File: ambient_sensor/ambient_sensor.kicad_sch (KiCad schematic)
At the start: 13 parts, among them J1 Conn_01x02_Pin, U4 ATmega328-P, U6 LD1117S33TR_SOT223, Y1 Crystal

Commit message: sensors connected
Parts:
- removed R1: 4.7k, symbol Device:R
- removed R2: 4.7k, Resistor_SMD:R_1206_3216Metric, symbol Device:R
- added BT1: Battery, Battery:BatteryHolder_Keystone_2479_3xAAA, symbol Device:Battery
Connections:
- net +4V: no longer U3.2 (3Vo)
- net GND: now also BT1.2 (-)
- net SDA: now reaches U2. (VIN), U4.27 (PC4)
- net SDA: now also U1.2 (SDA), U3.6 (SDI)
- net SCL: now reaches U1.3 (SCL), U2. (VIN), U4.28 (PC5)
- net SCL: now also U3.4 (SCK); no longer U3.5 (SDO)
- net at U6.3 (VI): now also BT1.1 (+)
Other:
- moved on the sheet: U1, U2, U3

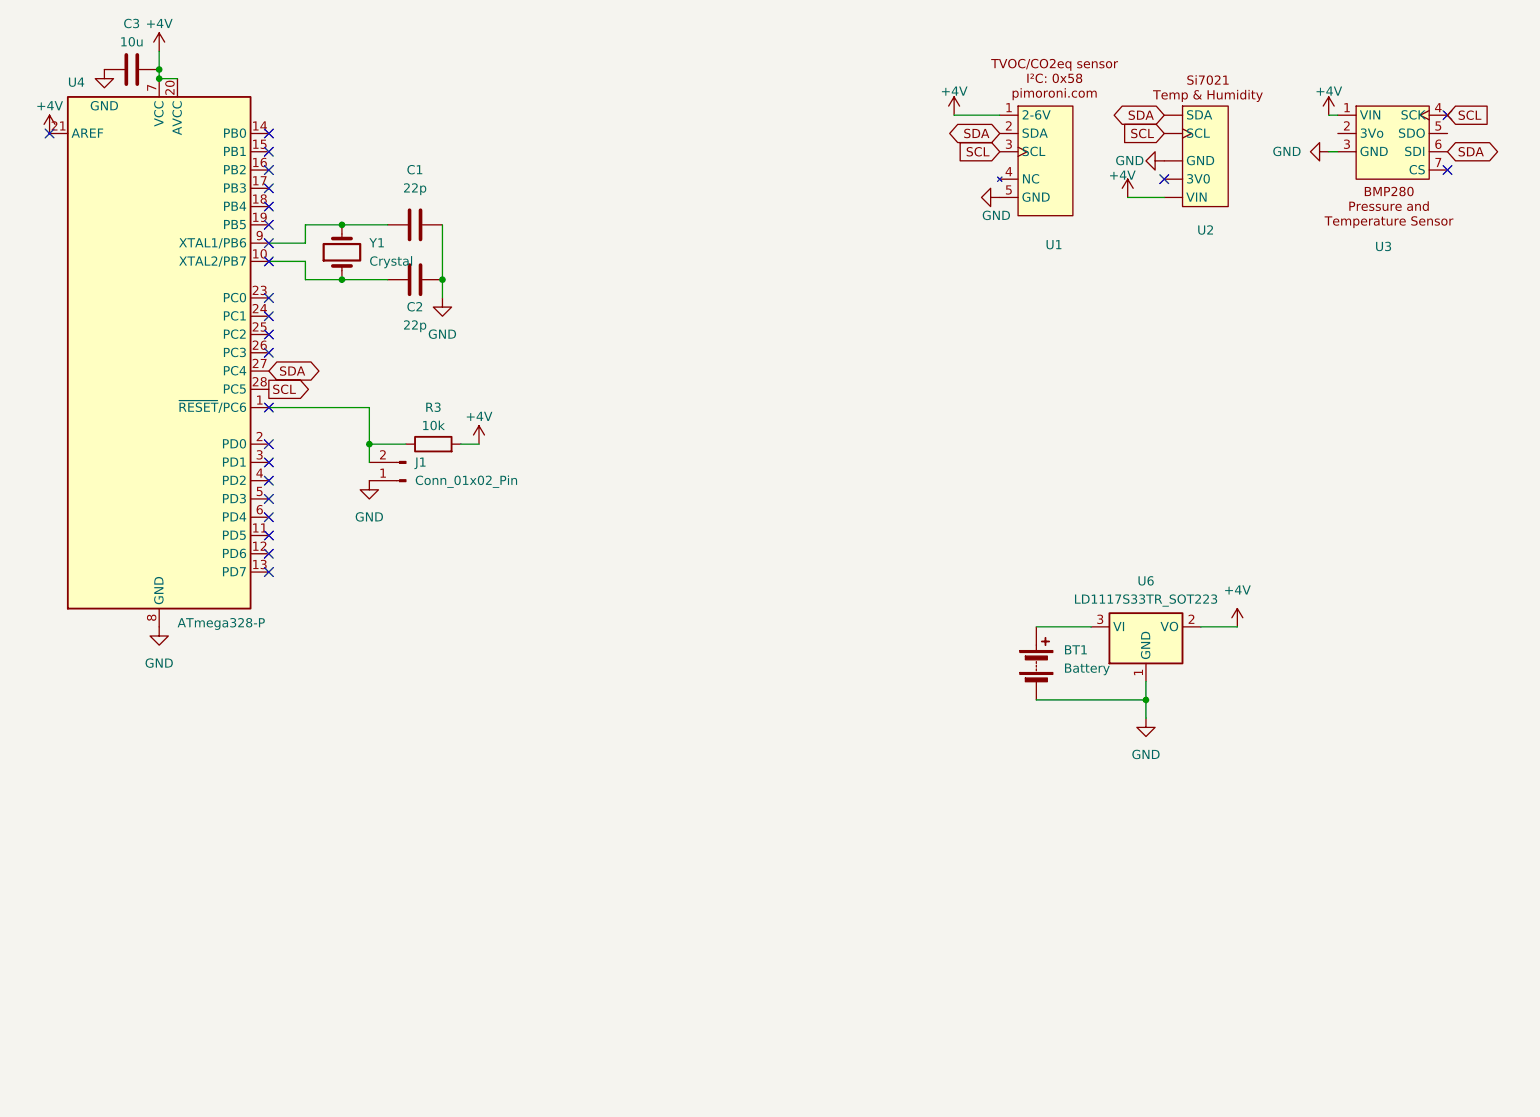
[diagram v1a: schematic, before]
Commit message: basic circuit is ready
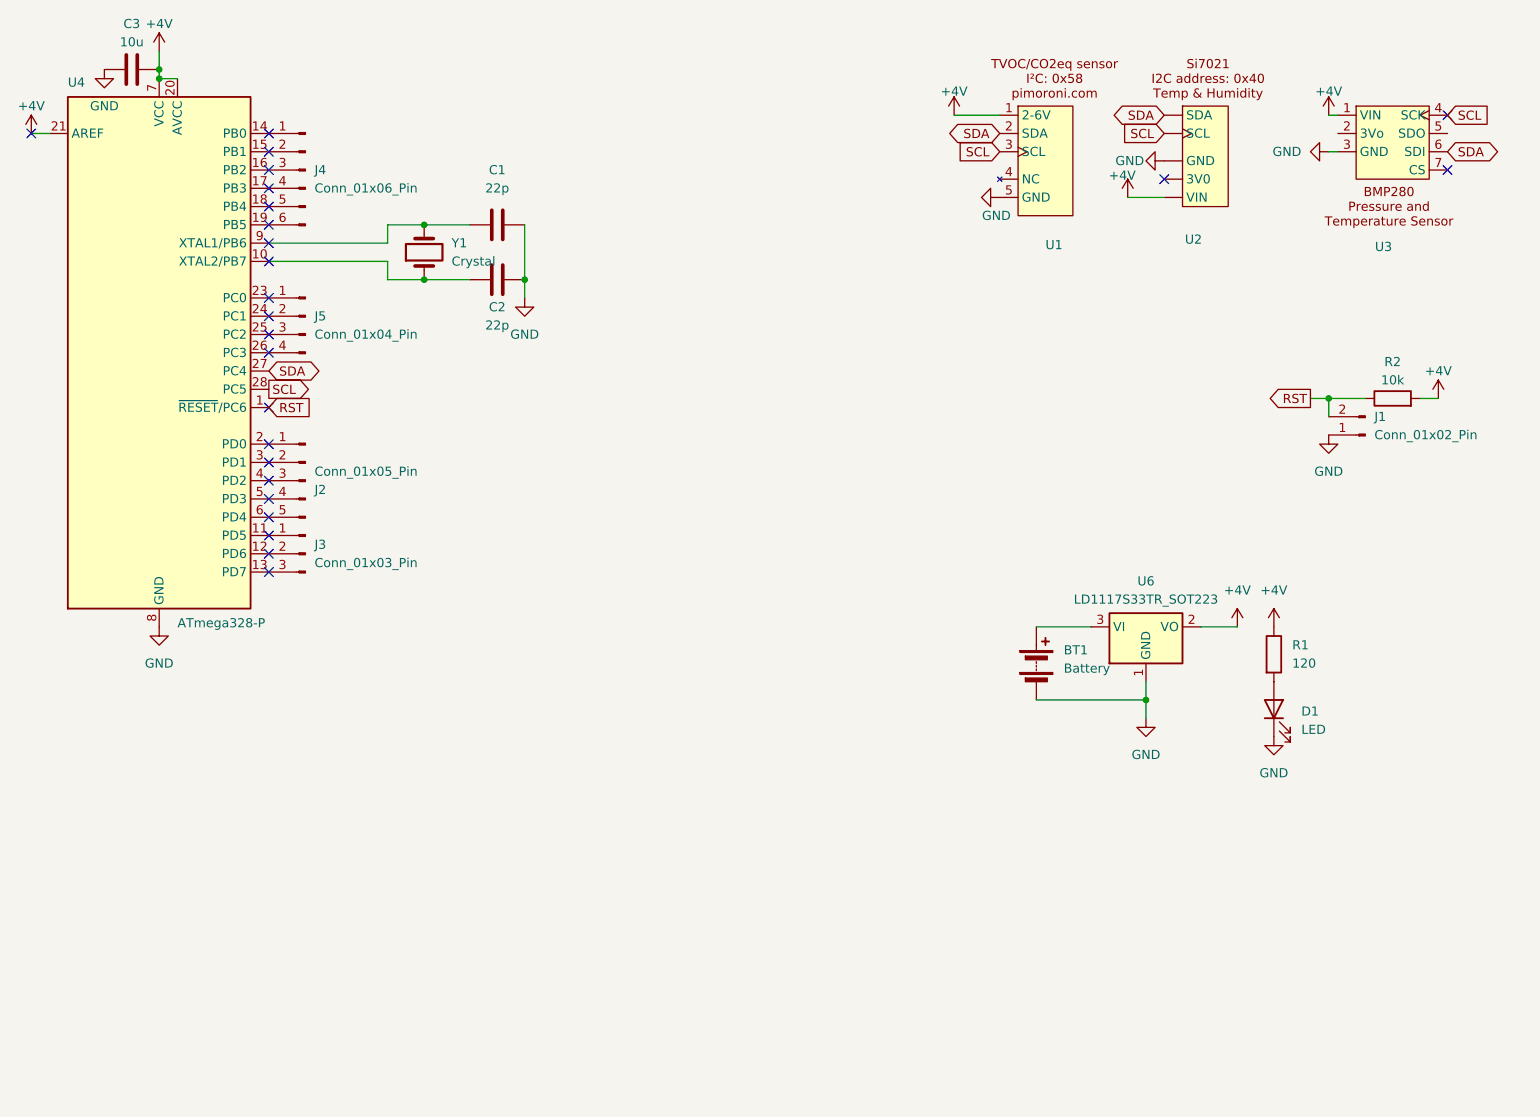
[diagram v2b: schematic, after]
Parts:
- added D1: LED, LED_SMD:LED_1206_3216Metric, symbol Device:LED
- added J2: Conn_01x05_Pin, Connector_PinHeader_2.54mm:PinHeader_1x05_P2.54mm_Vertical, symbol Connector:Conn_01x05_Pin
- added J3: Conn_01x03_Pin, Connector_PinHeader_2.54mm:PinHeader_1x03_P2.54mm_Vertical, symbol Connector:Conn_01x03_Pin
- added J4: Conn_01x06_Pin, Connector_PinHeader_2.54mm:PinHeader_1x06_P2.54mm_Vertical, symbol Connector:Conn_01x06_Pin
- added J5: Conn_01x04_Pin, Connector_PinHeader_2.54mm:PinHeader_1x04_P2.54mm_Vertical, symbol Connector:Conn_01x04_Pin
- added R1: 120, Resistor_SMD:R_1206_3216Metric, symbol Device:R
- BT1: footprint Battery:BatteryHolder_Keystone_2479_3xAAA -> (none)
- renumbered R3 to R2
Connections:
- net +4V: now also R1.1
- net GND: now also D1.1 (K)
- net RST: now reaches J1.2 (Pin_2), R2.1, U4.1 (~{RESET}/PC6)
- net at U4.11 (PD5): now also J3.1 (Pin_1)
- net at U4.12 (PD6): now also J3.2 (Pin_2)
- net at U4.13 (PD7): now also J3.3 (Pin_3)
- net at U4.14 (PB0): now also J4.1 (Pin_1)
- net at U4.15 (PB1): now also J4.2 (Pin_2)
- net at U4.16 (PB2): now also J4.3 (Pin_3)
- net at U4.17 (PB3): now also J4.4 (Pin_4)
- net at U4.18 (PB4): now also J4.5 (Pin_5)
- net at U4.19 (PB5): now also J4.6 (Pin_6)
- net at U4.2 (PD0): now also J2.1 (Pin_1)
- net at U4.23 (PC0): now also J5.1 (Pin_1)
- net at U4.24 (PC1): now also J5.2 (Pin_2)
- net at U4.25 (PC2): now also J5.3 (Pin_3)
- net at U4.26 (PC3): now also J5.4 (Pin_4)
- net at U4.3 (PD1): now also J2.2 (Pin_2)
- net at U4.4 (PD2): now also J2.3 (Pin_3)
- net at U4.5 (PD3): now also J2.4 (Pin_4)
- net at U4.6 (PD4): now also J2.5 (Pin_5)
- new net: D1.2 (A), R1.2
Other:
- company: (none) -> École Centrale de Lille
- title: (none) -> Indoor ambient sensor
- moved on the sheet: C1, C2, J1, R2, Y1

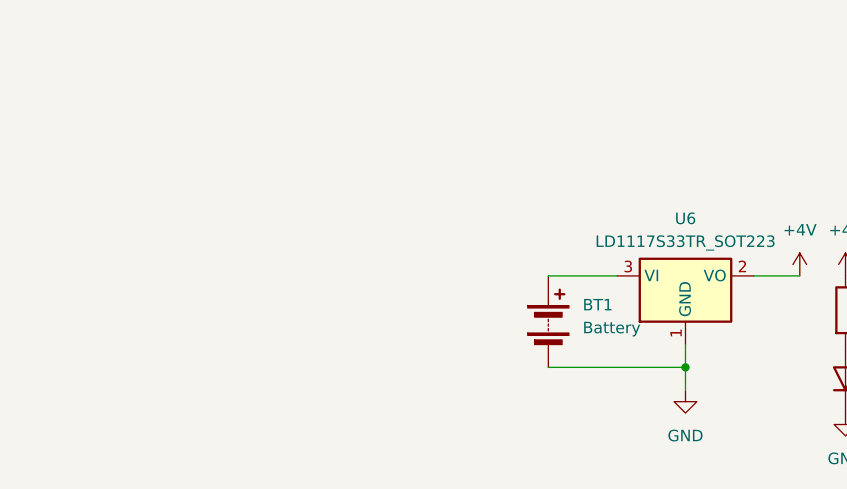
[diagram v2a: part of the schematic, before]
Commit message: rteverse voltage protection
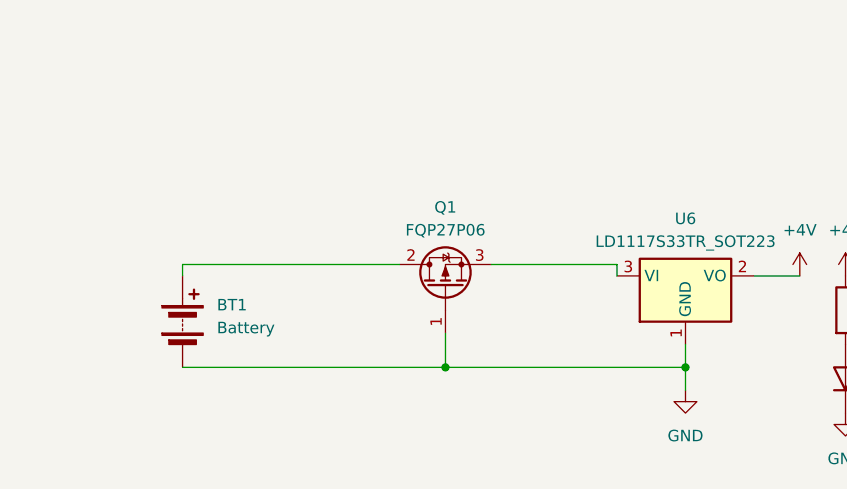
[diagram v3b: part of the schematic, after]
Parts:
- added Q1: FQP27P06, Package_TO_SOT_THT:TO-220-3_Vertical, symbol Transistor_FET:FQP27P06
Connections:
- net GND: now also Q1.1 (G)
- net at BT1.1 (+): now also Q1.2 (D); no longer U6.3 (VI)
- new net: Q1.3 (S), U6.3 (VI)
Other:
- moved on the sheet: BT1
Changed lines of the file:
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@@
+	)
+	(junction
+		(at 154.94 107.95)
+		(diameter 0)
+		(color 0 0 0 0)
 	)
 	(junction
@@
 	(wire
 		(pts
-			(xy 166.37 97.79) (xy 173.99 97.79)
-		)
-		(stroke
-			(width 0)
-			(type default)
-		)
-	)
-	(wire
-		(pts
-			(xy 166.37 107.95) (xy 181.61 107.95)
+			(xy 125.73 107.95) (xy 154.94 107.95)
 		)
 		(stroke
@@
 	(wire
 		(pts
+			(xy 160.02 96.52) (xy 173.99 96.52)
+		)
+		(stroke
+			(width 0)
+			(type default)
+		)
+	)
+	(wire
+		(pts
 			(xy 207.01 66.04) (xy 212.09 66.04)
 		)
@@
 	(wire
 		(pts
+			(xy 125.73 96.52) (xy 125.73 97.79)
+		)
+		(stroke
+			(width 0)
+			(type default)
+		)
+	)
+	(wire
+		(pts
 			(xy 76.2 49.53) (xy 76.2 46.99)
 		)
@@
 	(wire
 		(pts
+			(xy 154.94 107.95) (xy 181.61 107.95)
+		)
+		(stroke
+			(width 0)
+			(type default)
+		)
+	)
+	(wire
+		(pts
 			(xy 154.94 26.67) (xy 161.29 26.67)
 		)
@@
 	(wire
 		(pts
+			(xy 149.86 96.52) (xy 125.73 96.52)
+		)
+		(stroke
+			(width 0)
+			(type default)
+		)
+	)
+	(wire
+		(pts
+			(xy 173.99 96.52) (xy 173.99 97.79)
+		)
+		(stroke
+			(width 0)
+			(type default)
+		)
+	)
+	(wire
+		(pts
 			(xy 81.28 49.53) (xy 76.2 49.53)
+		)
+		(stroke
+			(width 0)
+			(type default)
+		)
+	)
+	(wire
+		(pts
+			(xy 154.94 104.14) (xy 154.94 107.95)
 		)
 		(stroke
@@
 	(symbol
 		(lib_id "Device:Battery")
-		(at 166.37 102.87 0)
+		(at 125.73 102.87 0)
 		(unit 1)
 		(exclude_from_sim no)
@@
 		(fields_autoplaced yes)
 		(property "Reference" "BT1"
-			(at 170.18 101.0284 0)
+			(at 129.54 101.0284 0)
 			(effects
 				(font
@@
 		)
 		(property "Value" "Battery"
-			(at 170.18 103.5684 0)
+			(at 129.54 103.5684 0)
 			(effects
 				(font
@@
 		)
 		(property "Footprint" ""
-			(at 166.37 101.346 90)
+			(at 125.73 101.346 90)
 			(effects
 				(font
@@
 		)
 		(property "Datasheet" "~"
-			(at 166.37 101.346 90)
+			(at 125.73 101.346 90)
 			(effects
 				(font
@@
 		)
 		(property "Description" "Multiple-cell battery"
-			(at 166.37 102.87 0)
+			(at 125.73 102.87 0)
 			(effects
 				(font
@@
 					(unit 1)
 				)
+			)
+		)
+	)
+	(symbol
+		(lib_id "Transistor_FET:FQP27P06")
+		(at 154.94 99.06 90)
+		(unit 1)
+		(exclude_from_sim no)
+		(in_bom yes)
+		(on_board yes)
+		(dnp no)
+		(fields_autoplaced yes)
+		(property "Reference" "Q1"
+			(at 154.94 90.17 90)
+			(effects
+				(font
+					(size 1.27 1.27)
+				)
+			)
+		)
+		(property "Value" "FQP27P06"
+			(at 154.94 92.71 90)
+			(effects
+				(font
+					(size 1.27 1.27)
+				)
+			)
+		)
+		(property "Footprint" "Package_TO_SOT_THT:TO-220-3_Vertical"
+			(at 156.845 93.98 0)
+			(effects
+				(font
+					(size 1.27 1.27)
+					(italic yes)
+				)
+				(justify left)
+				(hide yes)
+			)
+		)
+		(property "Datasheet" "https://www.onsemi.com/pub/Collateral/FQP27P06-D.PDF"
+			(at 158.75 93.98 0)
+			(effects
+				(font
+					(size 1.27 1.27)
+				)
+				(justify left)
+				(hide yes)
+			)
+		)
+		(property "Description" "-27A Id, -60V Vds, QFET P-Channel MOSFET, TO-220"
+			(at 154.94 99.06 0)
+			(effects
+				(font
+					(size 1.27 1.27)
+				)
+				(hide yes)
+			)
+		)
+		(pin "2"
+		)
+		(pin "3"
+		)
+		(pin "1"
+		)
+		(instances
+			(project ""
+				(path "/9e64b25d-56eb-4d28-941d-8d1b0cd0a88c"
+					(reference "Q1")
+					(unit 1)
+				)

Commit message: take away the protection
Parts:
- removed Q1: FQP27P06, Package_TO_SOT_THT:TO-220-3_Vertical, symbol Transistor_FET:FQP27P06
- added J6: Micro_SD_Card, symbol Connector:Micro_SD_Card
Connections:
- net at BT1.1 (+): now also U6.3 (VI)
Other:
- moved on the sheet: BT1
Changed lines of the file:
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@@
-	)
-	(junction
-		(at 154.94 107.95)
-		(diameter 0)
-		(color 0 0 0 0)
 	)
 	(junction
@@
 	(wire
 		(pts
-			(xy 125.73 107.95) (xy 154.94 107.95)
+			(xy 161.29 107.95) (xy 181.61 107.95)
 		)
 		(stroke
@@
 	(wire
 		(pts
-			(xy 160.02 96.52) (xy 173.99 96.52)
+			(xy 207.01 66.04) (xy 212.09 66.04)
 		)
 		(stroke
@@
 	(wire
 		(pts
-			(xy 207.01 66.04) (xy 212.09 66.04)
+			(xy 44.45 20.32) (xy 44.45 21.59)
 		)
 		(stroke
@@
 	(wire
 		(pts
-			(xy 44.45 20.32) (xy 44.45 21.59)
+			(xy 59.69 46.99) (xy 76.2 46.99)
 		)
 		(stroke
@@
 	(wire
 		(pts
-			(xy 59.69 46.99) (xy 76.2 46.99)
+			(xy 76.2 49.53) (xy 76.2 46.99)
 		)
 		(stroke
@@
 	(wire
 		(pts
-			(xy 125.73 96.52) (xy 125.73 97.79)
+			(xy 181.61 110.49) (xy 181.61 107.95)
 		)
 		(stroke
@@
 	(wire
 		(pts
-			(xy 76.2 49.53) (xy 76.2 46.99)
+			(xy 207.01 66.04) (xy 207.01 68.58)
 		)
 		(stroke
@@
 	(wire
 		(pts
-			(xy 181.61 110.49) (xy 181.61 107.95)
+			(xy 154.94 26.67) (xy 161.29 26.67)
 		)
 		(stroke
@@
 	(wire
 		(pts
-			(xy 207.01 66.04) (xy 207.01 68.58)
+			(xy 44.45 17.78) (xy 44.45 20.32)
 		)
 		(stroke
@@
 	(wire
 		(pts
-			(xy 154.94 107.95) (xy 181.61 107.95)
+			(xy 95.25 52.07) (xy 95.25 49.53)
 		)
 		(stroke
@@
 	(wire
 		(pts
-			(xy 154.94 26.67) (xy 161.29 26.67)
+			(xy 76.2 44.45) (xy 59.69 44.45)
 		)
 		(stroke
@@
 	(wire
 		(pts
-			(xy 44.45 17.78) (xy 44.45 20.32)
+			(xy 44.45 21.59) (xy 46.99 21.59)
 		)
 		(stroke
@@
 	(wire
 		(pts
-			(xy 95.25 52.07) (xy 95.25 49.53)
+			(xy 219.71 66.04) (xy 222.25 66.04)
 		)
 		(stroke
@@
 	(wire
 		(pts
-			(xy 76.2 44.45) (xy 59.69 44.45)
+			(xy 189.23 97.79) (xy 194.31 97.79)
 		)
 		(stroke
@@
 	(wire
 		(pts
-			(xy 44.45 21.59) (xy 46.99 21.59)
+			(xy 76.2 41.91) (xy 76.2 44.45)
 		)
 		(stroke
@@
 	(wire
 		(pts
-			(xy 219.71 66.04) (xy 222.25 66.04)
+			(xy 26.67 29.21) (xy 29.21 29.21)
 		)
 		(stroke
@@
 	(wire
 		(pts
-			(xy 189.23 97.79) (xy 194.31 97.79)
+			(xy 161.29 97.79) (xy 173.99 97.79)
 		)
 		(stroke
@@
 	(wire
 		(pts
-			(xy 76.2 41.91) (xy 76.2 44.45)
-		)
-		(stroke
-			(width 0)
-			(type default)
-		)
-	)
-	(wire
-		(pts
-			(xy 26.67 29.21) (xy 29.21 29.21)
-		)
-		(stroke
-			(width 0)
-			(type default)
-		)
-	)
-	(wire
-		(pts
-			(xy 149.86 96.52) (xy 125.73 96.52)
-		)
-		(stroke
-			(width 0)
-			(type default)
-		)
-	)
-	(wire
-		(pts
-			(xy 173.99 96.52) (xy 173.99 97.79)
-		)
-		(stroke
-			(width 0)
-			(type default)
-		)
-	)
-	(wire
-		(pts
 			(xy 81.28 49.53) (xy 76.2 49.53)
-		)
-		(stroke
-			(width 0)
-			(type default)
-		)
-	)
-	(wire
-		(pts
-			(xy 154.94 104.14) (xy 154.94 107.95)
 		)
 		(stroke
@@
 	(symbol
 		(lib_id "Device:Battery")
-		(at 125.73 102.87 0)
+		(at 161.29 102.87 0)
 		(unit 1)
 		(exclude_from_sim no)
@@
 		(fields_autoplaced yes)
 		(property "Reference" "BT1"
-			(at 129.54 101.0284 0)
+			(at 165.1 101.0284 0)
 			(effects
 				(font
@@
 		)
 		(property "Value" "Battery"
-			(at 129.54 103.5684 0)
+			(at 165.1 103.5684 0)
 			(effects
 				(font
@@
 		)
 		(property "Footprint" ""
-			(at 125.73 101.346 90)
+			(at 161.29 101.346 90)
 			(effects
 				(font
@@
 		)
 		(property "Datasheet" "~"
-			(at 125.73 101.346 90)
+			(at 161.29 101.346 90)
 			(effects
 				(font
@@
 		)
 		(property "Description" "Multiple-cell battery"
-			(at 125.73 102.87 0)
+			(at 161.29 102.87 0)
 			(effects
 				(font
@@
 				(path "/9e64b25d-56eb-4d28-941d-8d1b0cd0a88c"
 					(reference "BT1")
-					(unit 1)
-				)
-			)
-		)
-	)
-	(symbol
-		(lib_id "Transistor_FET:FQP27P06")
-		(at 154.94 99.06 90)
-		(unit 1)
-		(exclude_from_sim no)
-		(in_bom yes)
-		(on_board yes)
-		(dnp no)
-		(fields_autoplaced yes)
-		(property "Reference" "Q1"
-			(at 154.94 90.17 90)
-			(effects
-				(font
-					(size 1.27 1.27)
-				)
-			)
-		)
-		(property "Value" "FQP27P06"
-			(at 154.94 92.71 90)
-			(effects
-				(font
-					(size 1.27 1.27)
-				)
-			)
-		)
-		(property "Footprint" "Package_TO_SOT_THT:TO-220-3_Vertical"
-			(at 156.845 93.98 0)
-			(effects
-				(font
-					(size 1.27 1.27)
-					(italic yes)
-				)
-				(justify left)
-				(hide yes)
-			)
-		)
-		(property "Datasheet" "https://www.onsemi.com/pub/Collateral/FQP27P06-D.PDF"
-			(at 158.75 93.98 0)
-			(effects
-				(font
-					(size 1.27 1.27)
-				)
-				(justify left)
-				(hide yes)
-			)
-		)
-		(property "Description" "-27A Id, -60V Vds, QFET P-Channel MOSFET, TO-220"
-			(at 154.94 99.06 0)
-			(effects
-				(font
-					(size 1.27 1.27)
-				)
-				(hide yes)
-			)
-		)
-		(pin "2"
-		)
-		(pin "3"
-		)
-		(pin "1"
-		)
-		(instances
-			(project ""
-				(path "/9e64b25d-56eb-4d28-941d-8d1b0cd0a88c"
-					(reference "Q1")
 					(unit 1)
 				)
@@
 	)
 	(symbol
+		(lib_id "Connector:Micro_SD_Card")
+		(at 106.68 147.32 0)
+		(unit 1)
+		(exclude_from_sim no)
+		(in_bom yes)
+		(on_board yes)
+		(dnp no)
+		(fields_autoplaced yes)
+		(property "Reference" "J6"
+			(at 107.315 128.27 0)
+			(effects
+				(font
+					(size 1.27 1.27)
+				)
+			)
+		)
+		(property "Value" "Micro_SD_Card"
+			(at 107.315 130.81 0)
+			(effects
+				(font
+					(size 1.27 1.27)
+				)
+			)
+		)
+		(property "Footprint" ""
+			(at 135.89 139.7 0)
+			(effects
+				(font
+					(size 1.27 1.27)
+				)
+				(hide yes)
+			)
+		)
+		(property "Datasheet" "https://www.we-online.com/components/products/datasheet/693072010801.pdf"
+			(at 106.68 147.32 0)
+			(effects
+				(font
+					(size 1.27 1.27)
+				)
+				(hide yes)
+			)
+		)
+		(property "Description" "Micro SD Card Socket"
+			(at 106.68 147.32 0)
+			(effects
+				(font
+					(size 1.27 1.27)
+				)
+				(hide yes)
+			)
+		)
+		(pin "8"
+		)
+		(pin "9"
+		)
+		(pin "7"
+		)
+		(pin "2"
+		)
+		(pin "4"
+		)
+		(pin "5"
+		)
+		(pin "1"
+		)
+		(pin "6"
+		)
+		(pin "3"
+		)
+		(instances
+			(project ""
+				(path "/9e64b25d-56eb-4d28-941d-8d1b0cd0a88c"
+					(reference "J6")
+					(unit 1)
+				)
+			)
+		)
+	)
+	(symbol
 		(lib_id "power:GND")
 		(at 36.83 20.32 0)
@@
 		(dnp no)
 		(property "Reference" "U3"
-			(at 214.63 44.958 0)
+			(at 214.63 45.72 0)
 			(effects
 				(font
@@
 		)
 		(property "Value" "~"
-			(at 215.392 24.13 0)
-			(effects
-				(font
+			(at 214.63 45.72 0)
+			(effects
+				(font
